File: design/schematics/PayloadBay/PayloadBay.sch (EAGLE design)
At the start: 30 parts, among them IC1 MC33269ST-5.0T3, IC2 MC33269D-5.0, IC3 ATMEGA2560-16AU, Q1 MOSFET-PCHANNELFQP27P06, Q2 16MHz, X1 DC21MMX, Y1 16MHz

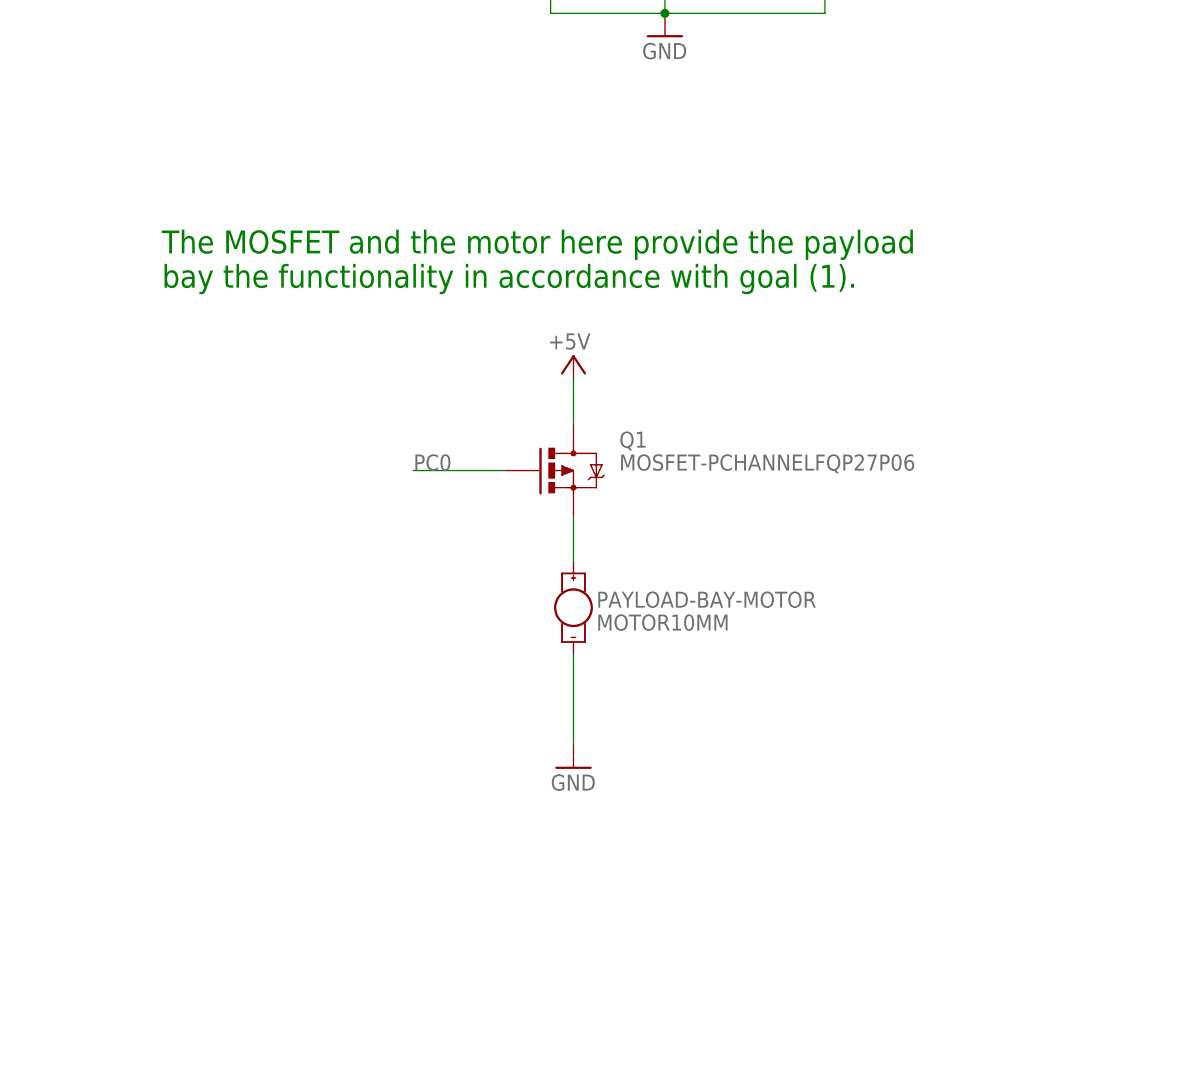
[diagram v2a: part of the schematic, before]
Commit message: fixed lack of motor control
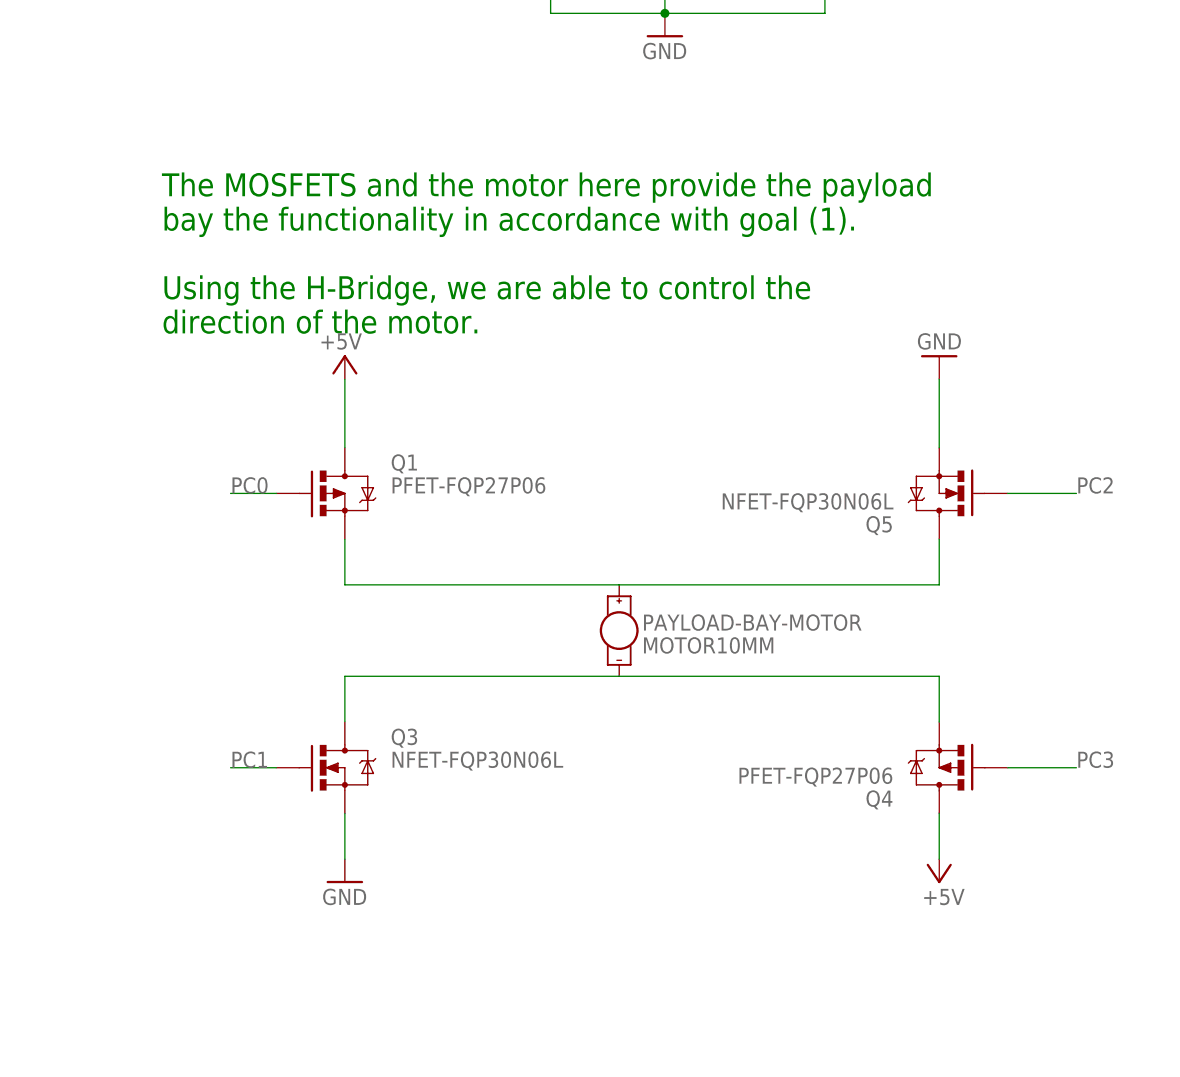
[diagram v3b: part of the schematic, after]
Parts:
- added Q3, Q5: NFET-FQP30N06L, SparkFun-DiscreteSemi:MOSFET-NCHANNELFQP30N06L
- added Q4: PFET-FQP27P06, SparkFun-DiscreteSemi:MOSFET-PCHANNELFQP27P06
- Q1: value MOSFET-PCHANNELFQP27P06 -> PFET-FQP27P06
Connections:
- new net N$4: PAYLOAD-BAY-MOTOR.-, Q3.D, Q4.S
- net +5V: now also Q4.D
- net GND: now also Q3.S, Q5.S; no longer PAYLOAD-BAY-MOTOR.-
- net N$1: now also Q5.D
- net PC0: no longer Q1.G
- net PC1: now also Q3.G
- net PC2: now also Q5.G
- net PC3: now also Q4.G
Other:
- note added: "The MOSFETS and the motor here provide the payload bay the functionality in accordance with goal (1). Using the H-Bridge, we are able to control the direction of the motor."
- note removed: "The MOSFET and the motor here provide the payload bay the functionality in accordance with goal (1)."
- moved on the sheet: PAYLOAD-BAY-MOTOR, Q1
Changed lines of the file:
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@@
 <part name="LIMIT-OPEN" library="SparkFun-Electromechanical" deviceset="SWITCH-MOMENTARY-2" device="12MM" value="2 Terminal Limit Switch"/>
 <part name="LIMIT-CLOSED" library="SparkFun-Electromechanical" deviceset="SWITCH-MOMENTARY-2" device="12MM" value="2 Terminal Limit Switch"/>
-<part name="Q1" library="SparkFun-DiscreteSemi" deviceset="MOSFET-PCHANNEL" device="FQP27P06"/>
 <part name="PAYLOAD-BAY-MOTOR" library="SparkFun-Electromechanical" deviceset="MOTOR" device="10MM"/>
 <part name="P+2" library="supply1" deviceset="+5V" device=""/>
@@
 <part name="P+4" library="supply1" deviceset="+5V" device=""/>
 <part name="GND4" library="supply1" deviceset="GND" device=""/>
+<part name="Q4" library="SparkFun-DiscreteSemi" deviceset="MOSFET-PCHANNEL" device="FQP27P06" value="PFET-FQP27P06"/>
+<part name="Q1" library="SparkFun-DiscreteSemi" deviceset="MOSFET-PCHANNEL" device="FQP27P06" value="PFET-FQP27P06"/>
+<part name="GND5" library="supply1" deviceset="GND" device=""/>
+<part name="P+6" library="supply1" deviceset="+5V" device=""/>
+<part name="Q3" library="SparkFun-DiscreteSemi" deviceset="MOSFET-NCHANNEL" device="FQP30N06L" value="NFET-FQP30N06L"/>
+<part name="Q5" library="SparkFun-DiscreteSemi" deviceset="MOSFET-NCHANNEL" device="FQP30N06L" value="NFET-FQP30N06L"/>
 </parts>
 <sheets>
@@
 The reed switch allows a magnet to provide control
 input to the payload bay system to switch states.</text>
-<text x="137.16" y="12.7" size="2.54" layer="91">The MOSFET and the motor here provide the payload
+<text x="137.16" y="7.62" size="2.54" layer="91">The MOSFETS and the motor here provide the payload
 bay the functionality in accordance with goal (1).
+Using the H-Bridge, we are able to control the
+direction of the motor.
 </text>
 </plain>
@@
 <instance part="LIMIT-OPEN" gate="G$1" x="162.56" y="101.6"/>
 <instance part="LIMIT-CLOSED" gate="G$1" x="162.56" y="83.82"/>
-<instance part="Q1" gate="G$1" x="182.88" y="-7.62"/>
-<instance part="PAYLOAD-BAY-MOTOR" gate="G$1" x="182.88" y="-22.86"/>
-<instance part="P+2" gate="1" x="182.88" y="5.08" smashed="yes">
-<attribute name="VALUE" x="184.785" y="7.62" size="1.778" layer="96" rot="R180"/>
-</instance>
-<instance part="GND3" gate="1" x="182.88" y="-40.64"/>
+<instance part="PAYLOAD-BAY-MOTOR" gate="G$1" x="187.96" y="-25.4"/>
+<instance part="P+2" gate="1" x="157.48" y="5.08" smashed="yes">
+<attribute name="VALUE" x="159.385" y="7.62" size="1.778" layer="96" rot="R180"/>
+</instance>
+<instance part="GND3" gate="1" x="157.48" y="-53.34"/>
 <instance part="P+4" gate="1" x="152.4" y="111.76" smashed="yes">
 <attribute name="VALUE" x="154.305" y="114.3" size="1.778" layer="96" rot="R180"/>
 </instance>
 <instance part="GND4" gate="1" x="193.04" y="40.64"/>
+<instance part="Q4" gate="G$1" x="223.52" y="-40.64" rot="R180"/>
+<instance part="Q1" gate="G$1" x="157.48" y="-10.16"/>
+<instance part="GND5" gate="1" x="223.52" y="5.08" rot="R180"/>
+<instance part="P+6" gate="1" x="223.52" y="-53.34" smashed="yes" rot="R180">
+<attribute name="VALUE" x="221.615" y="-55.88" size="1.778" layer="96"/>
+</instance>
+<instance part="Q3" gate="G$1" x="157.48" y="-40.64"/>
+<instance part="Q5" gate="G$1" x="223.52" y="-10.16" rot="R180"/>
 </instances>
 <busses>
@@
 </segment>
 <segment>
+<pinref part="Q1" gate="G$1" pin="D"/>
 <pinref part="P+2" gate="1" pin="+5V"/>
-<pinref part="Q1" gate="G$1" pin="D"/>
-<wire x1="182.88" y1="-2.54" x2="182.88" y2="2.54" width="0.1524" layer="91"/>
+<wire x1="157.48" y1="-5.08" x2="157.48" y2="2.54" width="0.1524" layer="91"/>
+</segment>
+<segment>
+<pinref part="Q4" gate="G$1" pin="D"/>
+<pinref part="P+6" gate="1" pin="+5V"/>
+<wire x1="223.52" y1="-45.72" x2="223.52" y2="-50.8" width="0.1524" layer="91"/>
 </segment>
 </net>
@@
 </segment>
 <segment>
-<pinref part="PAYLOAD-BAY-MOTOR" gate="G$1" pin="-"/>
+<pinref part="GND5" gate="1" pin="GND"/>
+<pinref part="Q5" gate="G$1" pin="S"/>
+<wire x1="223.52" y1="2.54" x2="223.52" y2="-5.08" width="0.1524" layer="91"/>
+</segment>
+<segment>
 <pinref part="GND3" gate="1" pin="GND"/>
-<wire x1="182.88" y1="-38.1" x2="182.88" y2="-27.94" width="0.1524" layer="91"/>
+<pinref part="Q3" gate="G$1" pin="S"/>
+<wire x1="157.48" y1="-50.8" x2="157.48" y2="-45.72" width="0.1524" layer="91"/>
 </segment>
 </net>
@@
 </segment>
 <segment>
-<pinref part="Q1" gate="G$1" pin="G"/>
-<wire x1="175.26" y1="-7.62" x2="165.1" y2="-7.62" width="0.1524" layer="91"/>
-<label x="165.1" y="-7.62" size="1.778" layer="95"/>
+<wire x1="149.86" y1="-10.16" x2="144.78" y2="-10.16" width="0.1524" layer="91"/>
+<label x="144.78" y="-10.16" size="1.778" layer="95"/>
 </segment>
 </net>
@@
 <pinref part="IC3" gate="1" pin="(A9)PC1"/>
 </segment>
+<segment>
+<pinref part="Q3" gate="G$1" pin="G"/>
+<wire x1="149.86" y1="-40.64" x2="144.78" y2="-40.64" width="0.1524" layer="91"/>
+<label x="144.78" y="-40.64" size="1.778" layer="95"/>
+</segment>
 </net>
 <net name="PC2" class="0">
@@
 <pinref part="IC3" gate="1" pin="(A10)PC2"/>
 </segment>
+<segment>
+<pinref part="Q5" gate="G$1" pin="G"/>
+<wire x1="231.14" y1="-10.16" x2="238.76" y2="-10.16" width="0.1524" layer="91"/>
+<label x="238.76" y="-10.16" size="1.778" layer="95"/>
+</segment>
 </net>
 <net name="PC3" class="0">
@@
 <label x="55.245" y="5.715" size="1.778" layer="95"/>
 <pinref part="IC3" gate="1" pin="(A11)PC3"/>
+</segment>
+<segment>
+<pinref part="Q4" gate="G$1" pin="G"/>
+<wire x1="231.14" y1="-40.64" x2="238.76" y2="-40.64" width="0.1524" layer="91"/>
+<label x="238.76" y="-40.64" size="1.778" layer="95"/>
 </segment>
 </net>
@@
 <net name="N$1" class="0">
 <segment>
+<pinref part="Q1" gate="G$1" pin="S"/>
 <pinref part="PAYLOAD-BAY-MOTOR" gate="G$1" pin="+"/>
-<pinref part="Q1" gate="G$1" pin="S"/>
-<wire x1="182.88" y1="-17.78" x2="182.88" y2="-12.7" width="0.1524" layer="91"/>
-</segment>
-</net>
+<wire x1="157.48" y1="-15.24" x2="157.48" y2="-20.32" width="0.1524" layer="91"/>
+<wire x1="157.48" y1="-20.32" x2="187.96" y2="-20.32" width="0.1524" layer="91"/>
+<pinref part="Q5" gate="G$1" pin="D"/>
+<wire x1="187.96" y1="-20.32" x2="223.52" y2="-20.32" width="0.1524" layer="91"/>
+<wire x1="223.52" y1="-20.32" x2="223.52" y2="-15.24" width="0.1524" layer="91"/>
+</segment>
+</net>
+<net name="N$4" class="0">
+<segment>
+<pinref part="Q3" gate="G$1" pin="D"/>
+<pinref part="PAYLOAD-BAY-MOTOR" gate="G$1" pin="-"/>
+<wire x1="157.48" y1="-35.56" x2="157.48" y2="-30.48" width="0.1524" layer="91"/>
+<wire x1="157.48" y1="-30.48" x2="187.96" y2="-30.48" width="0.1524" layer="91"/>
+<pinref part="Q4" gate="G$1" pin="S"/>
+<wire x1="187.96" y1="-30.48" x2="223.52" y2="-30.48" width="0.1524" layer="91"/>
+<wire x1="223.52" y1="-30.48" x2="223.52" y2="-35.56" width="0.1524" layer="91"/>
+</segment>
+</net>
